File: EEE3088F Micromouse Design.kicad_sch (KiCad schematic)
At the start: 86 parts, among them J1 Conn_02x16_Odd_Even, J2 Conn_01x02, J3 TYPE-C-31-M-12, Q1 AO3400A, U1 INA219AxD, U10 BQ24650, U11 DRV8833PW, U12 DRV8833PW, U13 AP22966DC8-7, U2 DRV8837, U3 DRV8837, U4 DRV8837, U5 DRV8837, U6 TPS5430DDA, U7 TPS61088RHLR, U8 MCP73833-xxx-MF, U9 CH224K

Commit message: Added 9V -> 5V Buck Converter to feed regulated 5V to Charging IC
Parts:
- removed C23: C_Small, symbol Device:C_Small
- removed R21, R22: 13k, Resistor_SMD:R_1206_3216Metric_Pad1.30x1.75mm_HandSolder, symbol Device:R_Small_US
- added C39: 180μF, Capacitor_SMD:C_1206_3216Metric_Pad1.33x1.80mm_HandSolder, symbol Device:C_Small
- added C40: 180uF 35V, Capacitor_SMD:CP_Elec_5x3, symbol Device:C_Polarized_Small_US
- added D2: 1N5820, Diode_THT:D_DO-201AD_P15.24mm_Horizontal, symbol Diode:1N5820
- added L3: 68uH/2A, symbol Device:L
- added U14: XL1509-5.0, Package_SO:SOIC-8_3.9x4.9mm_P1.27mm, symbol Regulator_Switching:XL1509-5.0
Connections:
- net GND: now also C39.1, C40.2, D2.2 (A), U14.4 (~{EN}), U14.5 (GND), U14.6 (GND), U14.7 (GND), U14.8 (GND)
- net HV: now also C39.2, U14.1 (VIN)
- net at U8.1 (V_{DD}), U8.2 (V_{DD}): now also C40.1, L3.2, U14.3 (FB)
- new net: D2.1 (K), L3.1, U14.2 (OUT)
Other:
- note added: "5V Battey Charger"
- note added: "9V -> 5V Buck Converter"
- moved on the sheet: C25, C26, Q1, R10, R11, R12, R13, R17, R18, R19, R20, R23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

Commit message: Added parallel resistor combination for 500mA motor. Easier E12 configuration and cheaper
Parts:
- removed R27, R28: 0.4, Resistor_SMD:R_1206_3216Metric_Pad1.30x1.75mm_HandSolder, symbol Device:R_Small_US
- added R29, R30, R31, R32: 0.82, Resistor_SMD:R_0603_1608Metric_Pad0.98x0.95mm_HandSolder, symbol Device:R_Small_US
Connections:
- net GND: now also R29.2, R30.2, R31.2, R32.2
- net at U12.6 (BISEN): now also R29.1, R30.1
- net at U12.3 (AISEN): now also R31.1, R32.1
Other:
- moved on the sheet: C30, C31, C32, U12

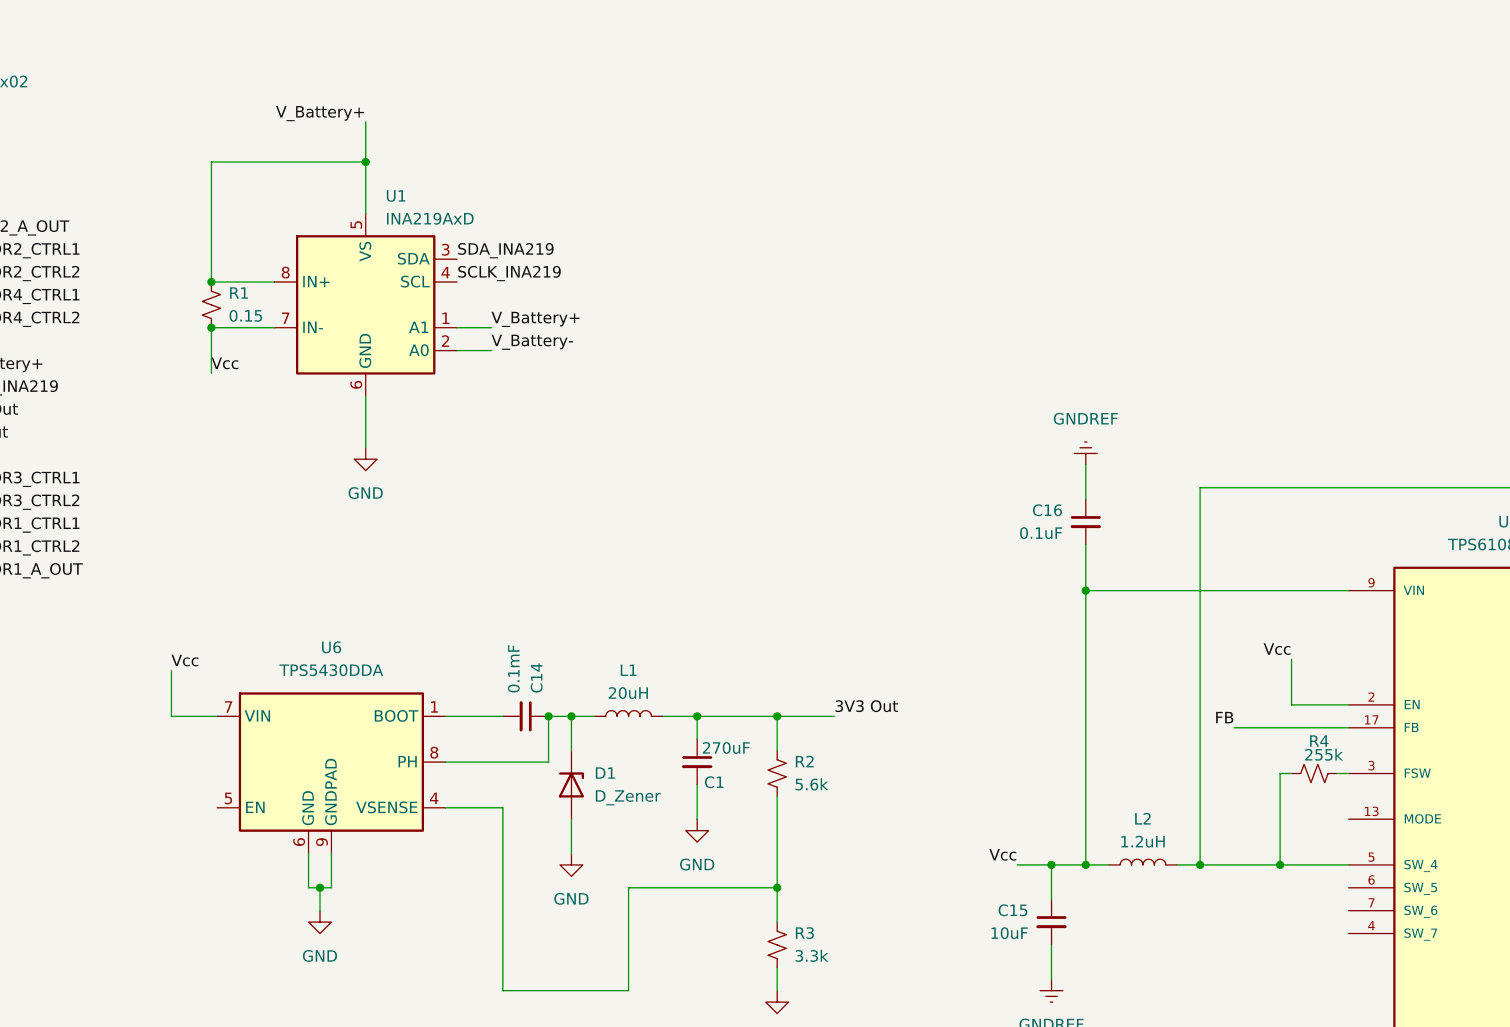
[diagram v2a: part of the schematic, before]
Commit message: Added switch changed some stuff to be E12
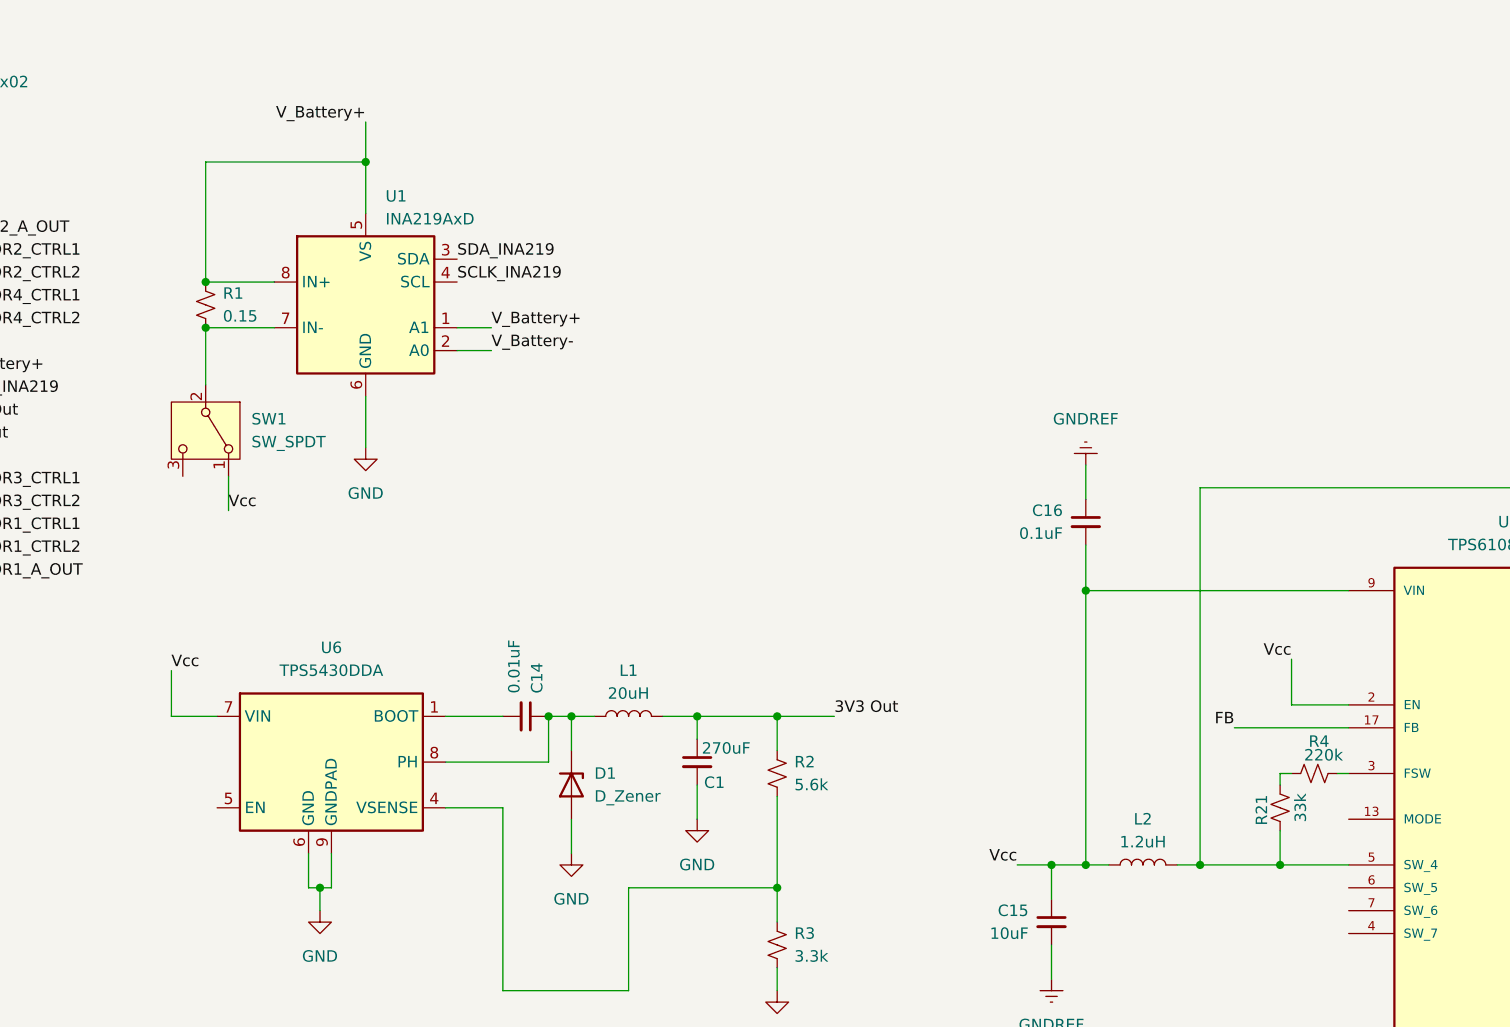
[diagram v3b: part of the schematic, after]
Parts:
- added R21: 33k, Resistor_SMD:R_1206_3216Metric_Pad1.30x1.75mm_HandSolder, symbol Device:R_Small_US
- added SW1: SW_SPDT, symbol Switch:SW_SPDT
- C14: value 0.1mF -> 0.01uF
- R4: value 255k -> 220k
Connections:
- net Vcc: now also SW1.1 (A); no longer R1.1, U1.7 (IN-)
- net at C17.2, L2.2, U7.5 (SW_4): now also R21.1; no longer R4.2
- new net: R21.2, R4.2
- new net: R1.1, SW1.2 (B), U1.7 (IN-)
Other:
- moved on the sheet: R1
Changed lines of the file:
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@@
 	)
 	(junction
-		(at 73.025 41.91)
+		(at 72.39 41.91)
 		(diameter 0)
 		(color 0 0 0 0)
@@
 	)
 	(junction
-		(at 73.025 46.99)
+		(at 72.39 46.99)
 		(diameter 0)
 		(color 0 0 0 0)
@@
 	(wire
 		(pts
+			(xy 191.77 102.87) (xy 191.77 106.68)
+		)
+		(stroke
+			(width 0)
+			(type default)
+		)
+	)
+	(wire
+		(pts
 			(xy 478.79 97.79) (xy 478.79 106.68)
 		)
@@
 	(wire
 		(pts
-			(xy 73.025 46.99) (xy 73.025 52.07)
-		)
-		(stroke
-			(width 0)
-			(type default)
-		)
-	)
-	(wire
-		(pts
 			(xy 85.09 109.22) (xy 85.09 111.76)
 		)
@@
 	(wire
 		(pts
-			(xy 73.025 28.575) (xy 90.17 28.575)
+			(xy 72.39 28.575) (xy 90.17 28.575)
 		)
 		(stroke
@@
 	(wire
 		(pts
+			(xy 72.39 46.99) (xy 72.39 53.34)
+		)
+		(stroke
+			(width 0)
+			(type default)
+		)
+	)
+	(wire
+		(pts
 			(xy 135.89 118.11) (xy 135.89 120.65)
 		)
@@
 	(wire
 		(pts
-			(xy 73.025 46.99) (xy 80.01 46.99)
+			(xy 72.39 46.99) (xy 80.01 46.99)
 		)
 		(stroke
@@
 	(wire
 		(pts
-			(xy 73.025 41.91) (xy 80.01 41.91)
+			(xy 72.39 41.91) (xy 80.01 41.91)
 		)
 		(stroke
@@
 	(wire
 		(pts
-			(xy 191.77 96.52) (xy 191.77 106.68)
+			(xy 191.77 96.52) (xy 191.77 97.79)
 		)
 		(stroke
@@
 	(wire
 		(pts
+			(xy 74.93 63.5) (xy 74.93 67.31)
+		)
+		(stroke
+			(width 0)
+			(type default)
+		)
+	)
+	(wire
+		(pts
 			(xy 234.95 91.44) (xy 256.54 91.44)
 		)
@@
 	(wire
 		(pts
-			(xy 73.025 41.91) (xy 73.025 28.575)
+			(xy 72.39 41.91) (xy 72.39 28.575)
 		)
 		(stroke
@@
 		)
 	)
-	(label "Vcc"
-		(at 73.025 52.07 0)
-		(effects
-			(font
-				(size 1.27 1.27)
-			)
-			(justify left bottom)
-		)
-	)
 	(label "Motor2_B_OUT"
 		(at 31.75 36.83 180)
@@
 		)
 	)
+	(label "Vcc"
+		(at 74.93 67.31 0)
+		(effects
+			(font
+				(size 1.27 1.27)
+			)
+			(justify left bottom)
+		)
+	)
 	(label "MOTOR2_CTRL1"
 		(at 532.13 63.5 180)
@@
 			)
 		)
-		(property "Value" "255k"
+		(property "Value" "220k"
 			(at 196.596 94.488 90)
 			(effects
@@
 	)
 	(symbol
+		(lib_id "Device:R_Small_US")
+		(at 191.77 100.33 180)
+		(unit 1)
+		(exclude_from_sim no)
+		(in_bom yes)
+		(on_board yes)
+		(dnp no)
+		(property "Reference" "R21"
+			(at 189.738 100.584 90)
+			(effects
+				(font
+					(size 1.27 1.27)
+				)
+			)
+		)
+		(property "Value" "33k"
+			(at 194.056 100.33 90)
+			(effects
+				(font
+					(size 1.27 1.27)
+				)
+			)
+		)
+		(property "Footprint" "Resistor_SMD:R_1206_3216Metric_Pad1.30x1.75mm_HandSolder"
+			(at 191.77 100.33 0)
+			(effects
+				(font
+					(size 1.27 1.27)
+				)
+				(hide yes)
+			)
+		)
+		(property "Datasheet" "~"
+			(at 191.77 100.33 0)
+			(effects
+				(font
+					(size 1.27 1.27)
+				)
+				(hide yes)
+			)
+		)
+		(property "Description" ""
+			(at 191.77 100.33 0)
+			(effects
+				(font
+					(size 1.27 1.27)
+				)
+			)
+		)
+		(pin "1"
+		)
+		(pin "2"
+		)
+		(instances
+			(project "EEE3088F Micromouse Design"
+				(path "/9da86a77-c081-4eef-8f80-aa4f3cdcfcf8"
+					(reference "R21")
+					(unit 1)
+				)
+			)
+		)
+	)
+	(symbol
 		(lib_id "power:GND")
 		(at 369.57 125.73 0)
@@
 	)
 	(symbol
+		(lib_id "Switch:SW_SPDT")
+		(at 72.39 58.42 270)
+		(unit 1)
+		(exclude_from_sim no)
+		(in_bom yes)
+		(on_board yes)
+		(dnp no)
+		(fields_autoplaced yes)
+		(property "Reference" "SW1"
+			(at 77.47 57.1499 90)
+			(effects
+				(font
+					(size 1.27 1.27)
+				)
+				(justify left)
+			)
+		)
+		(property "Value" "SW_SPDT"
+			(at 77.47 59.6899 90)
+			(effects
+				(font
+					(size 1.27 1.27)
+				)
+				(justify left)
+			)
+		)
+		(property "Footprint" ""
+			(at 72.39 58.42 0)
+			(effects
+				(font
+					(size 1.27 1.27)
+				)
+				(hide yes)
+			)
+		)
+		(property "Datasheet" "~"
+			(at 64.77 58.42 0)
+			(effects
+				(font
+					(size 1.27 1.27)
+				)
+				(hide yes)
+			)
+		)
+		(property "Description" "Switch, single pole double throw"
+			(at 72.39 58.42 0)
+			(effects
+				(font
+					(size 1.27 1.27)
+				)
+				(hide yes)
+			)
+		)
+		(pin "1"
+		)
+		(pin "3"
+		)
+		(pin "2"
+		)
+		(instances
+			(project ""
+				(path "/9da86a77-c081-4eef-8f80-aa4f3cdcfcf8"
+					(reference "SW1")
+					(unit 1)
+				)
+			)
+		)
+	)
+	(symbol
 		(lib_id "Device:R_Small_US")
 		(at 551.18 209.55 0)
@@
 	(symbol
 		(lib_id "Device:R_Small_US")
-		(at 73.025 44.45 180)
+		(at 72.39 44.45 180)
 		(unit 1)
 		(exclude_from_sim no)
@@
 		(fields_autoplaced yes)
 		(property "Reference" "R1"
-			(at 74.93 43.18 0)
+			(at 74.295 43.18 0)
 			(effects
 				(font
@@
 		)
 		(property "Value" "0.15"
-			(at 74.93 45.72 0)
+			(at 74.295 45.72 0)
 			(effects
 				(font
@@
 		)
 		(property "Footprint" "Resistor_SMD:R_1206_3216Metric_Pad1.30x1.75mm_HandSolder"
-			(at 73.025 44.45 0)
+			(at 72.39 44.45 0)
 			(effects
 				(font
@@
 		)
 		(property "Datasheet" "~"
-			(at 73.025 44.45 0)
+			(at 72.39 44.45 0)
 			(effects
 				(font
@@
 		)
 		(property "Description" ""
-			(at 73.025 44.45 0)
+			(at 72.39 44.45 0)
 			(effects
 				(font
@@
 			)
 		)
-		(property "Value" "0.1mF"
+		(property "Value" "0.01uF"
 			(at 106.6738 87.63 0)
 			(effects

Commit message: Changed Battery Charger to single IC and reformatted components
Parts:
- removed D2: 1N5820, Diode_THT:D_DO-201AD_P15.24mm_Horizontal, symbol Diode:1N5820
- added C23: 100uF, symbol Device:C_Small
- added C41: 47uF, symbol Device:C_Small
- added C42: 10uF, symbol Device:C_Small
- added D3: SS32, Diode_SMD:D_SMA, symbol Diode:SS32
- added Q2: AO3400A, Package_TO_SOT_SMD:SOT-23, symbol Transistor_FET:AO3400A
- added R22: 10k, Resistor_SMD:R_1206_3216Metric_Pad1.30x1.75mm_HandSolder, symbol Device:R_Small_US
- added R27: 4.7k, Resistor_SMD:R_1206_3216Metric_Pad1.30x1.75mm_HandSolder, symbol Device:R_Small_US
- added R28: 330, Resistor_SMD:R_1206_3216Metric_Pad1.30x1.75mm_HandSolder, symbol Device:R_Small_US
- added R33: 2.2k, Resistor_SMD:R_1206_3216Metric_Pad1.30x1.75mm_HandSolder, symbol Device:R_Small_US
- added R34: 270, Resistor_SMD:R_1206_3216Metric_Pad1.30x1.75mm_HandSolder, symbol Device:R_Small_US
- added U15: TP4056-42-ESOP8, Package_SO:SOIC-8-1EP_3.9x4.9mm_P1.27mm_EP2.41x3.3mm_ThermalVias, symbol Battery_Management:TP4056-42-ESOP8
- C1: value 270uF -> 100uF
- C39: value 180μF -> 100μF
- R1: value 0.15 -> 0.1
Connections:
- net 3V3 Out: now also C23.1, C41.1
- net FAST_CHARGE_CTRL: now also Q2.1 (G)
- net GND: now also C23.2, C41.2, C42.2, D3.2 (A), R22.2, U15.3 (GND), U15.9 (EPAD)
- net HV: now also U15.4 (V_{CC}), U15.8 (CE)
- net V_Battery+: now also C42.1, U15.5 (BAT)
- net at L3.1, U14.2 (OUT): now also D3.1 (K)
- new net: R27.2, R28.1
- new net: R28.2, R34.2
- new net: R33.2, R34.1
- new net: Q2.3 (D), R27.1, U15.2 (PROG)
- new net: Q2.2 (S), R33.1
- new net: R22.1, U15.1 (TEMP)
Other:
- moved on the sheet: C1, C14, C25, C26, C33, C34, C35, C36, C37, C38, C39, C40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

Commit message: Removed the graveyard and restructured board
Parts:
- removed C10, C11, C12, C13, C2, C3, C4, C5, C6, C7, C8, C9: 0.1mF, Capacitor_SMD:C_0402_1005Metric_Pad0.74x0.62mm_HandSolder, symbol Device:C_Small
- removed C25: 1uF, symbol Device:C_Small
- removed C26: 22pF, symbol Device:C_Small
- removed C39: 100μF, Capacitor_SMD:C_1206_3216Metric_Pad1.33x1.80mm_HandSolder, symbol Device:C_Small
- removed C40: 180uF 35V, Capacitor_SMD:CP_Elec_5x3, symbol Device:C_Polarized_Small_US
- removed D3: SS32, Diode_SMD:D_SMA, symbol Diode:SS32
- removed L3: 68uH/2A, symbol Device:L
- removed Q1: AO3400A, Package_TO_SOT_SMD:SOT-23, symbol Transistor_FET:AO3400A
- removed R10: 330, Resistor_SMD:R_1206_3216Metric_Pad1.30x1.75mm_HandSolder, symbol Device:R_Small_US
- removed R11: 2.2k, Resistor_SMD:R_1206_3216Metric_Pad1.30x1.75mm_HandSolder, symbol Device:R_Small_US
- removed R12: 270, Resistor_SMD:R_1206_3216Metric_Pad1.30x1.75mm_HandSolder, symbol Device:R_Small_US
- removed R13: 10k, Resistor_SMD:R_1206_3216Metric_Pad1.30x1.75mm_HandSolder, symbol Device:R_Small_US
- removed R17: 87k, Resistor_SMD:R_1206_3216Metric_Pad1.30x1.75mm_HandSolder, symbol Device:R_Small_US
- removed R18: 13k, Resistor_SMD:R_1206_3216Metric_Pad1.30x1.75mm_HandSolder, symbol Device:R_Small_US
- removed R19, R20: 700, Resistor_SMD:R_1206_3216Metric_Pad1.30x1.75mm_HandSolder, symbol Device:R_Small_US
- removed R23, R24: 100, Resistor_SMD:R_1206_3216Metric_Pad1.30x1.75mm_HandSolder, symbol Device:R_Small_US
- removed R9: 4.7k, Resistor_SMD:R_1206_3216Metric_Pad1.30x1.75mm_HandSolder, symbol Device:R_Small_US
- removed U10: BQ24650, Package_DFN_QFN:Texas_RVA_VQFN-16-1EP_3.5x3.5mm_P0.5mm_EP2.14x2.14mm_ThermalVias, symbol Battery_Management:BQ24650
- removed U14: XL1509-5.0, Package_SO:SOIC-8_3.9x4.9mm_P1.27mm, symbol Regulator_Switching:XL1509-5.0
- removed U2, U3, U4, U5: DRV8837, Package_SON:WSON-8-1EP_2x2mm_P0.5mm_EP0.9x1.6mm, symbol Driver_Motor:DRV8837
- removed U8: MCP73833-xxx-MF, Package_DFN_QFN:DFN-10-1EP_3x3mm_P0.5mm_EP1.58x2.35mm, symbol Battery_Management:MCP73833-xxx-MF
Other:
- note removed: "9V -> 5V Buck Converter"
- note removed: "GRAVEYARD OF DESIGNS (Remove When Populating Footprints)"
- moved on the sheet: C1, C14, C15, C16, C17, C18, C19, C20, C21, C22, C23, C24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

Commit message: Added items to BOM. Need to finish assignment
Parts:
- C19: value 22pF -> 1.5nF
- R6: value 10k -> 68k
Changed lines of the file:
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@@
 			)
 		)
-		(property "Value" "10k"
+		(property "Value" "68k"
 			(at 447.04 61.214 90)
 			(effects
@@
 			)
 		)
-		(property "Value" "22pF"
+		(property "Value" "1.5nF"
 			(at 459.994 60.452 90)
 			(effects

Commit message: Adding JLC part numbers
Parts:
- J1, J2: now not fitted
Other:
- note added: "3.3V Output Step down Buck Converter Circuit"
- note added: "5V Output Step Up Boost Converter"
- note added: "Battery Monitoring and Switching Circuit"
- note added: "USB-C Integration and Power Delivery Negotiation"
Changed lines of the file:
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@@
 	(generator_version "9.0")
 	(paper "A2")
+	(text "USB-C Integration and Power Delivery Negotiation"
+		(exclude_from_sim no)
+		(at 539.242 16.256 0)
+		(effects
+			(font
+				(size 1.27 1.27)
+			)
+		)
+	)
 	(text "200mA Motor"
 		(exclude_from_sim no)
@@
 		)
 	)
+	(text "5V Output Step Up Boost Converter\n\n "
+		(exclude_from_sim no)
+		(at 410.718 18.034 0)
+		(effects
+			(font
+				(size 1.27 1.27)
+			)
+		)
+	)
 	(text "5V Battey Charger"
 		(exclude_from_sim no)
@@
 		)
 	)
+	(text "3.3V Output Step down Buck Converter Circuit\n"
+		(exclude_from_sim no)
+		(at 257.302 18.542 0)
+		(effects
+			(font
+				(size 1.27 1.27)
+			)
+		)
+	)
+	(text "Battery Monitoring and Switching Circuit"
+		(exclude_from_sim no)
+		(at 139.954 16.256 0)
+		(effects
+			(font
+				(size 1.27 1.27)
+			)
+		)
+	)
 	(text "500mA Motor"
 		(exclude_from_sim no)
@@
 		(in_bom yes)
 		(on_board yes)
-		(dnp no)
+		(dnp yes)
 		(fields_autoplaced yes)
 		(property "Reference" "J1"
@@
 		(in_bom yes)
 		(on_board yes)
-		(dnp no)
+		(dnp yes)
 		(fields_autoplaced yes)
 		(property "Reference" "J2"
